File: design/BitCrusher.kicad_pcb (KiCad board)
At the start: 2 copper layers, 181.5 x 86.2 mm, 134 parts, among them J1 BNC, J10 PJ-002BH, J2 BWSMA-KWE-Z001, J3 BWSMA-KE-Z001, J4 BWSMA-KE-Z001, J5 SHOU HAN TYPE-C 14P CC-2.6, J6 Conn_01x04_Pin, J7 Conn_01x04_Pin, J8 Conn_01x03_Pin, J9 Conn_01x03_Pin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

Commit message: _
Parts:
- moved D2 1.28 mm to (222.2, 105.8), turned to -90 degrees
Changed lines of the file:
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@@
 		(tags "PJ-002B ")
 		(property "Reference" "J10"
-			(at 0 -3.17618 180)
+			(at 0.02325 2.39882 180)
 			(layer "F.SilkS")
 			(effects
@@
 	(footprint "Diode_SMD:D_SOD-882"
 		(layer "F.Cu")
-		(at 222.545 104.5)
+		(at 222.25 105.75 -90)
 		(descr "SOD-882, DFN1006-2, body 1.0 x 0.6 x 0.48mm, pitch 0.65mm, https://assets.nexperia.com/documents/package-information/SOD882.pdf")
 		(tags "Diode SOD882 DFN1006-2")
 		(property "Reference" "D2"
-			(at 0.13 1.25 180)
+			(at -1.5 0 180)
 			(layer "F.SilkS")
 			(effects
@@
 		)
 		(property "Value" "SP3031-01ETG"
-			(at 0 1.35 0)
+			(at 0 1.35 270)
 			(unlocked yes)
 			(layer "F.Fab")
@@
 		)
 		(property "Datasheet" "https://www.littelfuse.com/assetdocs/tvs-diode-arrays-sp3031-datasheet?assetguid=2f63a461-bb1a-458d-97ab-119532f3b1f4"
-			(at 0 0 0)
+			(at 0 0 270)
 			(unlocked yes)
 			(layer "F.Fab")
@@
 		)
 		(property "Description" "Bidirectional transient-voltage-suppression diode"
-			(at 0 0 0)
+			(at 0 0 270)
 			(unlocked yes)
 			(layer "F.Fab")
@@
 		)
 		(property "KLC_S4.2_3V3OUT" ""
-			(at 0 0 0)
+			(at 0 0 270)
 			(unlocked yes)
 			(layer "F.Fab")
@@
 		)
 		(property "KLC_S4.2_VCC" ""
-			(at 0 0 0)
+			(at 0 0 270)
 			(unlocked yes)
 			(layer "F.Fab")
@@
 		(attr smd)
 		(fp_line
-			(start -0.81 -0.61)
-			(end -0.81 0.61)
+			(start -0.81 0.61)
+			(end 0.5 0.61)
 			(stroke
 				(width 0.12)
@@
 		(fp_line
 			(start -0.81 -0.61)
-			(end 0.5 -0.61)
+			(end -0.81 0.61)
 			(stroke
 				(width 0.12)
@@
 		)
 		(fp_line
-			(start -0.81 0.61)
-			(end 0.5 0.61)
+			(start -0.81 -0.61)
+			(end 0.5 -0.61)
 			(stroke
 				(width 0.12)
@@
 		)
 		(fp_line
-			(start -0.8 -0.6)
+			(start 0.8 0.6)
 			(end -0.8 0.6)
 			(stroke
@@
 		(fp_line
 			(start -0.8 -0.6)
-			(end 0.8 -0.6)
+			(end -0.8 0.6)
 			(stroke
 				(width 0.05)
@@
 		)
 		(fp_line
-			(start 0.8 -0.6)
-			(end 0.8 0.6)
+			(start -0.8 -0.6)
+			(end 0.8 -0.6)
 			(stroke
 				(width 0.05)
@@
 		)
 		(fp_line
-			(start 0.8 0.6)
-			(end -0.8 0.6)
+			(start 0.8 -0.6)
+			(end 0.8 0.6)
 			(stroke
 				(width 0.05)
@@
 		)
 		(fp_line
-			(start -0.5 -0.3)
-			(end 0.5 -0.3)
+			(start -0.5 0.3)
+			(end -0.5 -0.3)
 			(stroke
 				(width 0.1)
@@
 		)
 		(fp_line
-			(start -0.5 0.3)
-			(end -0.5 -0.3)
+			(start 0.5 0.3)
+			(end -0.5 0.3)
 			(stroke
 				(width 0.1)
@@
 		)
 		(fp_line
-			(start -0.15 0)
-			(end -0.3 0)
+			(start -0.15 0.2)
+			(end -0.15 -0.2)
 			(stroke
 				(width 0.1)
@@
 		)
 		(fp_line
-			(start -0.15 0)
-			(end 0.15 0.2)
+			(start 0.15 0.2)
+			(end 0.15 -0.2)
 			(stroke
 				(width 0.1)
@@
 		)
 		(fp_line
-			(start -0.15 0.2)
-			(end -0.15 -0.2)
+			(start -0.15 0)
+			(end 0.15 0.2)
 			(stroke
 				(width 0.1)
@@
 		)
 		(fp_line
-			(start 0.15 -0.2)
-			(end -0.15 0)
+			(start -0.15 0)
+			(end -0.3 0)
 			(stroke
 				(width 0.1)
@@
 		)
 		(fp_line
-			(start 0.15 0.2)
-			(end 0.15 -0.2)
+			(start 0.15 -0.2)
+			(end -0.15 0)
 			(stroke
 				(width 0.1)
@@
 		)
 		(fp_line
-			(start 0.5 -0.3)
-			(end 0.5 0.3)
+			(start -0.5 -0.3)
+			(end 0.5 -0.3)
 			(stroke
 				(width 0.1)
@@
 		)
 		(fp_line
-			(start 0.5 0.3)
-			(end -0.5 0.3)
+			(start 0.5 -0.3)
+			(end 0.5 0.3)
 			(stroke
 				(width 0.1)
@@
 		)
 		(fp_text user "${REFERENCE}"
-			(at -0.127 -1.35 0)
+			(at -0.127 -1.35 270)
 			(unlocked yes)
 			(layer "F.Fab")
@@
 		)
 		(pad "" smd roundrect
-			(at -0.35 0)
+			(at -0.35 0 270)
 			(size 0.3 0.6)
 			(layers "F.Paste")
@@
 		)
 		(pad "" smd roundrect
-			(at 0.35 0)
+			(at 0.35 0 270)
 			(size 0.3 0.6)
 			(layers "F.Paste")
@@
 		)
 		(pad "1" smd roundrect
-			(at -0.35 0)
+			(at -0.35 0 270)
 			(size 0.4 0.7)
 			(layers "F.Cu" "F.Mask")
@@
 		)
 		(pad "2" smd roundrect
-			(at 0.35 0)
+			(at 0.35 0 270)
 			(size 0.4 0.7)
 			(layers "F.Cu" "F.Mask")
@@
 		(tags "TO-247-2 Horizontal RM 10.9mm")
 		(property "Reference" "RP_LIM1"
-			(at 5.45 -26.98 0)
+			(at 5.45 -3.61 0)
 			(layer "F.SilkS")
 			(effects
@@
 	)
 	(segment
-		(start 222.895 105.78)
-		(end 221.715 106.96)
+		(start 224.43 103.845)
+		(end 224.43 104.599953)
 		(width 0.5)
 		(layer "F.Cu")
@@
 	)
 	(segment
-		(start 221.715 106.96)
+		(start 221.39 106.96)
 		(end 217.175 106.96)
 		(width 0.5)
@@
 	)
 	(segment
-		(start 223.39 104.255)
-		(end 223.14 104.255)
-		(width 0.5)
-		(layer "F.Cu")
-		(net 19)
-	)
-	(segment
-		(start 223.14 104.255)
-		(end 222.895 104.5)
-		(width 0.5)
-		(layer "F.Cu")
-		(net 19)
-	)
-	(segment
 		(start 224.395 103.845)
 		(end 223.8 103.845)
@@
 	)
 	(segment
-		(start 222.895 104.5)
-		(end 222.895 105.78)
+		(start 222.25 106.1)
+		(end 221.39 106.96)
 		(width 0.5)
 		(layer "F.Cu")
@@
 	)
 	(segment
-		(start 223.39 104.255)
-		(end 223.8 103.845)
+		(start 224.43 104.599953)
+		(end 222.929953 106.1)
+		(width 0.5)
+		(layer "F.Cu")
+		(net 19)
+	)
+	(segment
+		(start 222.929953 106.1)
+		(end 222.25 106.1)
 		(width 0.5)
 		(layer "F.Cu")
@@
 	)
 	(segment
-		(start 219.795 104.5)
-		(end 219.715 104.42)
+		(start 222.25 116.6)
+		(end 222.25 117.295)
 		(width 0.5)
 		(layer "F.Cu")
@@
 	)
 	(segment
-		(start 222.25 116.6)
-		(end 222.25 117.295)
+		(start 222.25 105.4)
+		(end 221.35 104.5)
 		(width 0.5)
 		(layer "F.Cu")
@@
 	)
 	(segment
-		(start 222.195 104.5)
+		(start 221.35 104.5)
 		(end 219.795 104.5)
 		(width 0.5)
@@
 	)
 	(segment
+		(start 219.795 104.5)
+		(end 219.715 104.42)
+		(width 0.5)
+		(layer "F.Cu")
+		(net 21)
+	)
+	(segment
 		(start 222.25 117.295)
 		(end 219.715 119.83)
@@
 		(polygon
 			(pts
-				(xy 150.75 75.25) (xy 187.675 75.253061) (xy 188.925 76.503172) (xy 188.925 79.815672) (xy 187.9875 80.752429)
+				(xy 150.75 75.75) (xy 187.675 75.753061) (xy 188.925 77) (xy 188.925 79.815672) (xy 187.9875 80.752429)
 				(xy 184.925 80.75) (xy 183.425 81.752687) (xy 153 81.75) (xy 152 80.75) (xy 148.3 80.75) (xy 147.675 80.125)
 				(xy 147.675 76.375) (xy 148.3 75.75) (xy 150.175 75.75)
@@
 			(pts
 				(xy 191.661529 65.5) (xy 190.224029 66.9375) (xy 190.224029 70.171875) (xy 191.302154 71.25) (xy 193.056061 71.25)
-				(xy 194.25 72.5) (xy 194.25 76) (xy 194.25 76.75) (xy 195.974029 78.625) (xy 199.75 82.5) (xy 202.25 82.5)
-				(xy 203.75 81) (xy 203.75 79) (xy 202.5 77.75) (xy 200.724029 77.75) (xy 198.724029 75.75) (xy 198.724029 67.703125)
+				(xy 194.25 72.5) (xy 194.25 76.75) (xy 195.974029 78.625) (xy 199.75 82.5) (xy 202.25 82.5) (xy 203.75 81)
+				(xy 203.75 79) (xy 202.5 77.75) (xy 200.724029 77.75) (xy 198.724029 75.75) (xy 198.724029 67.703125)
 				(xy 196.520904 65.5)
 			)

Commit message: _
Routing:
- net Net-(D4-A): track 10.1 -> 0.00 mm
- net HV+: track 22.3 -> 19.1 mm
- added copper zone on F.Cu, net Net-(D4-A)
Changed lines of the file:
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@@
 	)
 	(segment
-		(start 157.955 102.50375)
-		(end 152.42125 102.50375)
+		(start 107.375 108.7)
+		(end 107.375 108.652081)
 		(width 0.5)
 		(layer "F.Cu")
@@
 	)
 	(segment
-		(start 143.75 111)
-		(end 109.675 111)
-		(width 0.5)
-		(layer "F.Cu")
-		(net 8)
-	)
-	(segment
-		(start 152.42125 102.50375)
-		(end 143.974 110.951)
-		(width 0.5)
-		(layer "F.Cu")
-		(net 8)
-	)
-	(segment
-		(start 158.25 102.79875)
-		(end 157.955 102.50375)
+		(start 109.675 111)
+		(end 107.375 108.7)
 		(width 0.5)
 		(layer "F.Cu")
@@
 	)
 	(segment
-		(start 109.675 111)
-		(end 107.375 108.7)
+		(start 156.24625 102.50375)
+		(end 147.75 111)
 		(width 0.5)
 		(layer "F.Cu")
@@
 	)
 	(segment
-		(start 143.799 110.951)
-		(end 143.75 111)
+		(start 157.955 102.50375)
+		(end 156.24625 102.50375)
 		(width 0.5)
 		(layer "F.Cu")
@@
 	)
 	(segment
-		(start 107.375 108.7)
-		(end 107.375 108.652081)
+		(start 158.25 102.79875)
+		(end 157.955 102.50375)
 		(width 0.5)
 		(layer "F.Cu")
@@
 	)
 	(segment
-		(start 143.974 110.951)
-		(end 143.799 110.951)
+		(start 147.75 111)
+		(end 109.675 111)
 		(width 0.5)
 		(layer "F.Cu")
@@
 	)
 	(segment
-		(start 103.575003 100.783626)
-		(end 103.575003 102.25)
+		(start 156.048068 101.54375)
+		(end 147.341818 110.25)
 		(width 0.5)
 		(layer "F.Cu")
@@
 	)
 	(segment
-		(start 158.475 101.02375)
-		(end 158.25 101.24875)
+		(start 158.25 101.24875)
+		(end 157.955 101.54375)
 		(width 0.5)
 		(layer "F.Cu")
@@
 	)
 	(segment
-		(start 102.796376 100.004999)
-		(end 103.575003 100.783626)
+		(start 103.575003 100.783626)
+		(end 103.575003 102.25)
 		(width 0.5)
 		(layer "F.Cu")
@@
 	)
 	(segment
-		(start 152.389886 101.54375)
-		(end 143.683636 110.25)
+		(start 158.475 101.02375)
+		(end 158.25 101.24875)
 		(width 0.5)
 		(layer "F.Cu")
@@
 	)
 	(segment
-		(start 103.575003 102.25)
-		(end 103.476 102.25)
+		(start 102.796376 100.004999)
+		(end 103.575003 100.783626)
 		(width 0.5)
 		(layer "F.Cu")
@@
 	)
 	(segment
-		(start 110.175 110.25)
-		(end 107.425 107.5)
+		(start 147.341818 110.25)
+		(end 110.175 110.25)
 		(width 0.5)
 		(layer "F.Cu")
@@
 	)
 	(segment
-		(start 157.955 101.54375)
-		(end 152.389886 101.54375)
+		(start 103.575003 102.25)
+		(end 103.476 102.25)
 		(width 0.5)
 		(layer "F.Cu")
@@
 	)
 	(segment
-		(start 158.25 101.24875)
-		(end 157.955 101.54375)
+		(start 157.955 101.54375)
+		(end 156.048068 101.54375)
 		(width 0.5)
 		(layer "F.Cu")
@@
 	)
 	(segment
-		(start 91.4625 100.4625)
-		(end 90.465 101.46)
-		(width 0.2)
+		(start 110.175 110.25)
+		(end 107.425 107.5)
+		(width 0.5)
 		(layer "F.Cu")
 		(net 9)
 	)
 	(segment
-		(start 143.683636 110.25)
-		(end 110.175 110.25)
-		(width 0.5)
+		(start 91.4625 100.4625)
+		(end 90.465 101.46)
+		(width 0.2)
 		(layer "F.Cu")
 		(net 9)
@@
 	)
 	(segment
-		(start 153.675 88.145)
-		(end 155.105 88.145)
-		(width 1)
-		(layer "F.Cu")
-		(net 20)
-	)
-	(segment
-		(start 155.105 88.145)
-		(end 155.5 87.75)
-		(width 1)
-		(layer "F.Cu")
-		(net 20)
-	)
-	(segment
 		(start 153.675 88.075)
 		(end 153.75 88)
@@
 	)
 	(segment
-		(start 155.5 87.75)
-		(end 155.5 84.725)
+		(start 180.675 84.55)
+		(end 185.2 84.55)
 		(width 1)
 		(layer "F.Cu")
@@
 	)
 	(segment
-		(start 180.675 84.55)
-		(end 185.2 84.55)
+		(start 155.675 86.377151)
+		(end 155.671984 86.380167)
 		(width 1)
 		(layer "F.Cu")
@@
 	)
 	(segment
+		(start 155.675 84.55)
+		(end 155.675 86.377151)
+		(width 1)
+		(layer "F.Cu")
+		(net 20)
+	)
+	(segment
 		(start 228.37 93)
 		(end 228.25 93)
@@
 	)
 	(segment
-		(start 149.025 100.3)
-		(end 149.025 96.795)
-		(width 2)
-		(layer "F.Cu")
-		(net 30)
-	)
-	(segment
-		(start 149.025 96.795)
-		(end 153.675 92.145)
-		(width 2)
-		(layer "F.Cu")
-		(net 30)
-	)
-	(segment
 		(start 124.998914 84.75)
 		(end 123.501086 83.252172)
@@
 	)
 	(zone
+		(net 30)
+		(net_name "Net-(D4-A)")
+		(layer "F.Cu")
+		(hatch edge 0.5)
+		(priority 18)
+		(connect_pads
+			(clearance 0.5)
+		)
+		(min_thickness 0.25)
+		(filled_areas_thickness no)
+		(fill yes
+			(thermal_gap 0.5)
+			(thermal_bridge_width 0.5)
+		)
+		(polygon
+			(pts
+				(xy 148.5 103) (xy 147.75 102.25) (xy 147.75 91.75) (xy 149.5 90) (xy 156 90) (xy 156.75 90.75)
+				(xy 156.75 97.5) (xy 151.25 103)
+			)
+		)
+	)
+	(zone
 		(net 119)
 		(net_name "GND")
@@
 				(xy 190.75 78.5) (xy 191.5 77.75) (xy 193.8125 77.75) (xy 194.5 78.5) (xy 194.5 86.25) (xy 193.75 87)
 				(xy 190.25 87) (xy 189 88.25) (xy 189 95.893203) (xy 188.293794 96.509255) (xy 183.749998 96.500917)
-				(xy 183.25 96) (xy 183.25 88.75) (xy 182.25 87.75) (xy 163.75 87.75) (xy 161 88.75) (xy 152 88.75)
+				(xy 183.25 96) (xy 183.25 88.75) (xy 182.25 87.75) (xy 165.75 87.75) (xy 163 88.75) (xy 152 88.75)
 				(xy 151.925 83.5)
 			)

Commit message: _
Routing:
- net Probe-: track 16.6 -> 1.31 mm

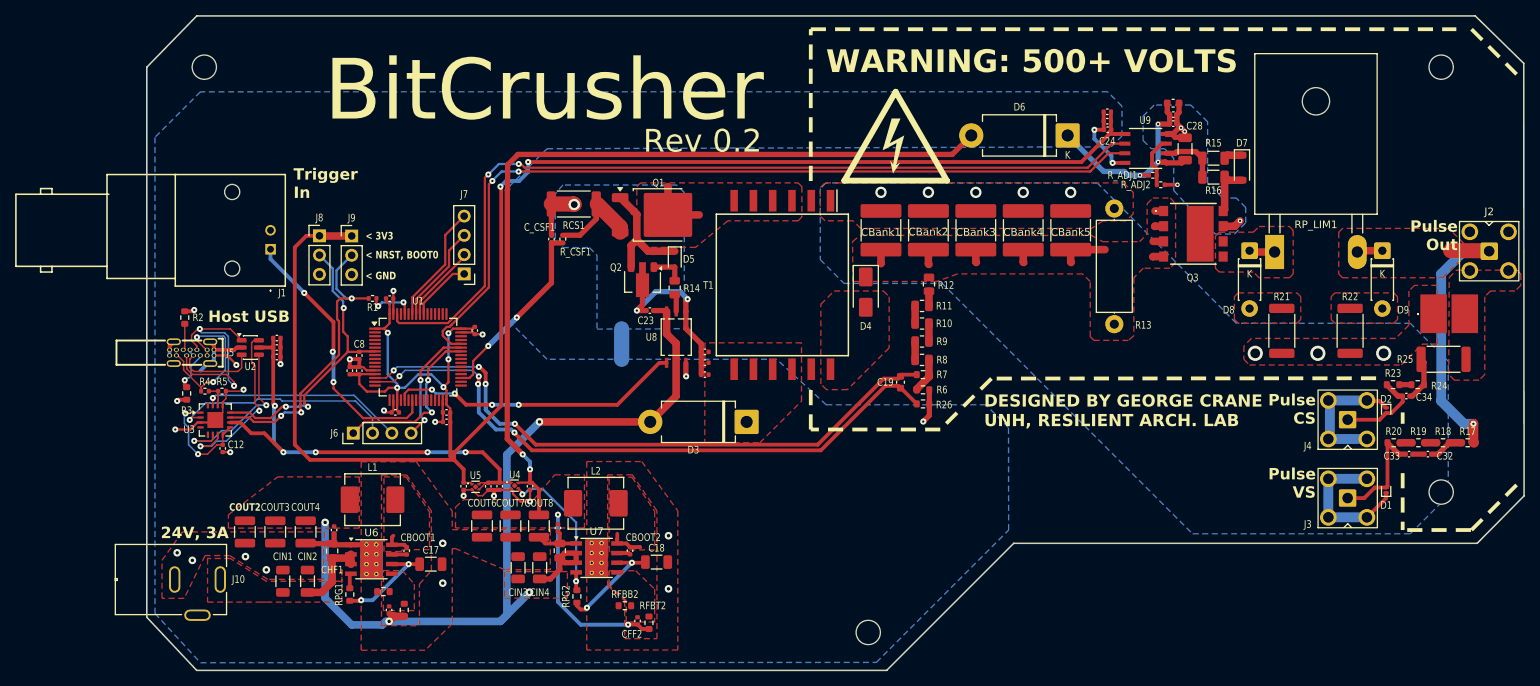
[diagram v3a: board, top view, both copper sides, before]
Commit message: added ferrite bead between HVGND and GND
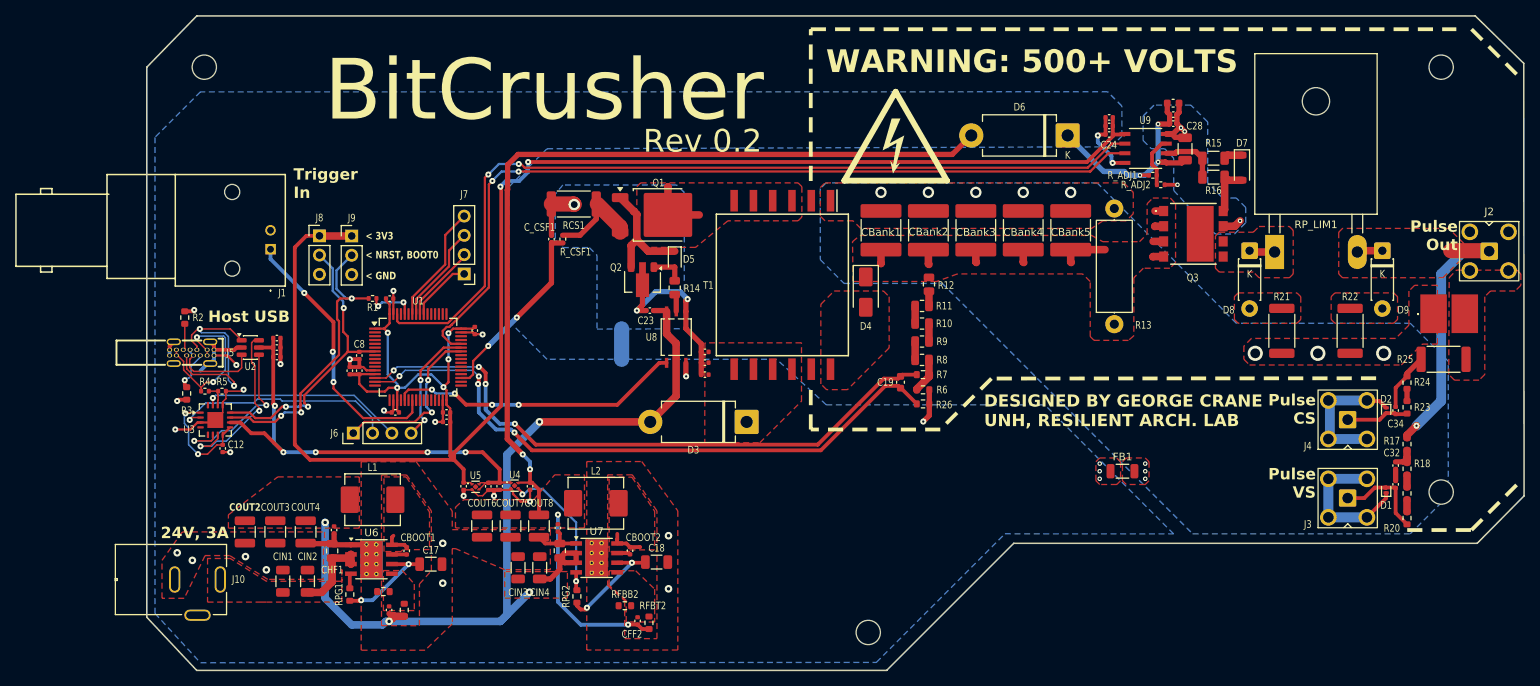
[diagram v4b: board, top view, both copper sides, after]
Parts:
- added FB1: CBW321609U101T, Inductor_SMD:L_1206_3216Metric, F.Cu at (187.5, 113.8)
- moved R20 10.1 mm to (225.0, 119.9), turned to -90 degrees
- moved R17 8.00 mm to (225.0, 110.2), turned to -90 degrees
- moved R19 6.84 mm to (225.0, 116.7), turned to -90 degrees
- moved R18 5.86 mm to (225.0, 113.4), turned to -90 degrees
- moved C32 4.51 mm to (223.5, 113.0), turned to 90 degrees
- moved C33 4.36 mm to (223.5, 115.5), turned to 90 degrees
- moved R23 3.50 mm to (225.0, 105.3), turned to 90 degrees
- moved C34 2.37 mm to (223.5, 105.8), turned to 90 degrees
- moved R24 1.44 mm to (225.0, 102.1), turned to 90 degrees
- moved C26 0.79 mm to (185.8, 67.1)
- moved C25 0.67 mm to (185.8, 68.2)
- moved C24 0.66 mm to (185.8, 69.4)
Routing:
- net PulseCS+: track 11.7 -> 8.27 mm
- net PulseVS+: track 14.6 -> 12.6 mm
- net Net-(C34-Pad2): track 6.06 -> 7.75 mm
- net Probe+: track 41.8 -> 40.5 mm
- net GND: track 100.5 -> 99.2 mm, vias 27 -> 30
- net Net-(C32-Pad2): track 4.57 -> 3.32 mm
- net +3V3: track 245.1 -> 244.4 mm
- net PulseCS-: vias 8 -> 11

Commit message: _
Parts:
- C14, C16: value 1u -> 5u
- C23: footprint Capacitor_SMD:C_0402_1005Metric -> Capacitor_SMD:C_1206_3216Metric
- moved C23 3.54 mm to (128.8, 92.5), turned to 0 degrees
- moved U8 2.06 mm to (128.7, 98.1)
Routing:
- net GNDFLY: track 33.4 -> 19.7 mm, vias 3 -> 4
- net GND: track 99.2 -> 94.7 mm
- net Net-(R14-Pad1): track 2.30 -> 4.36 mm
- net +22V: track 115.7 -> 114.1 mm
- net HVPWM: track 38.7 -> 37.9 mm

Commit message: _
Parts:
- moved NT1 2.00 mm to (123.5, 97.0)
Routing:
- net GND_DRV: track 14.2 -> 10.7 mm, vias 4 -> 7
- net PulseEN: track 111.1 -> 111.6 mm
- added copper zone on F.Cu, net GND_DRV
